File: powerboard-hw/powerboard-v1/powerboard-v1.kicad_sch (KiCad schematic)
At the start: 25 parts, among them J1 Conn_01x02, J2 PWR, J3 SIG, Q1 AO3401A, Q2 AO3400A, SW1 OS102011MA1Q, U1 TPS62842DGRR

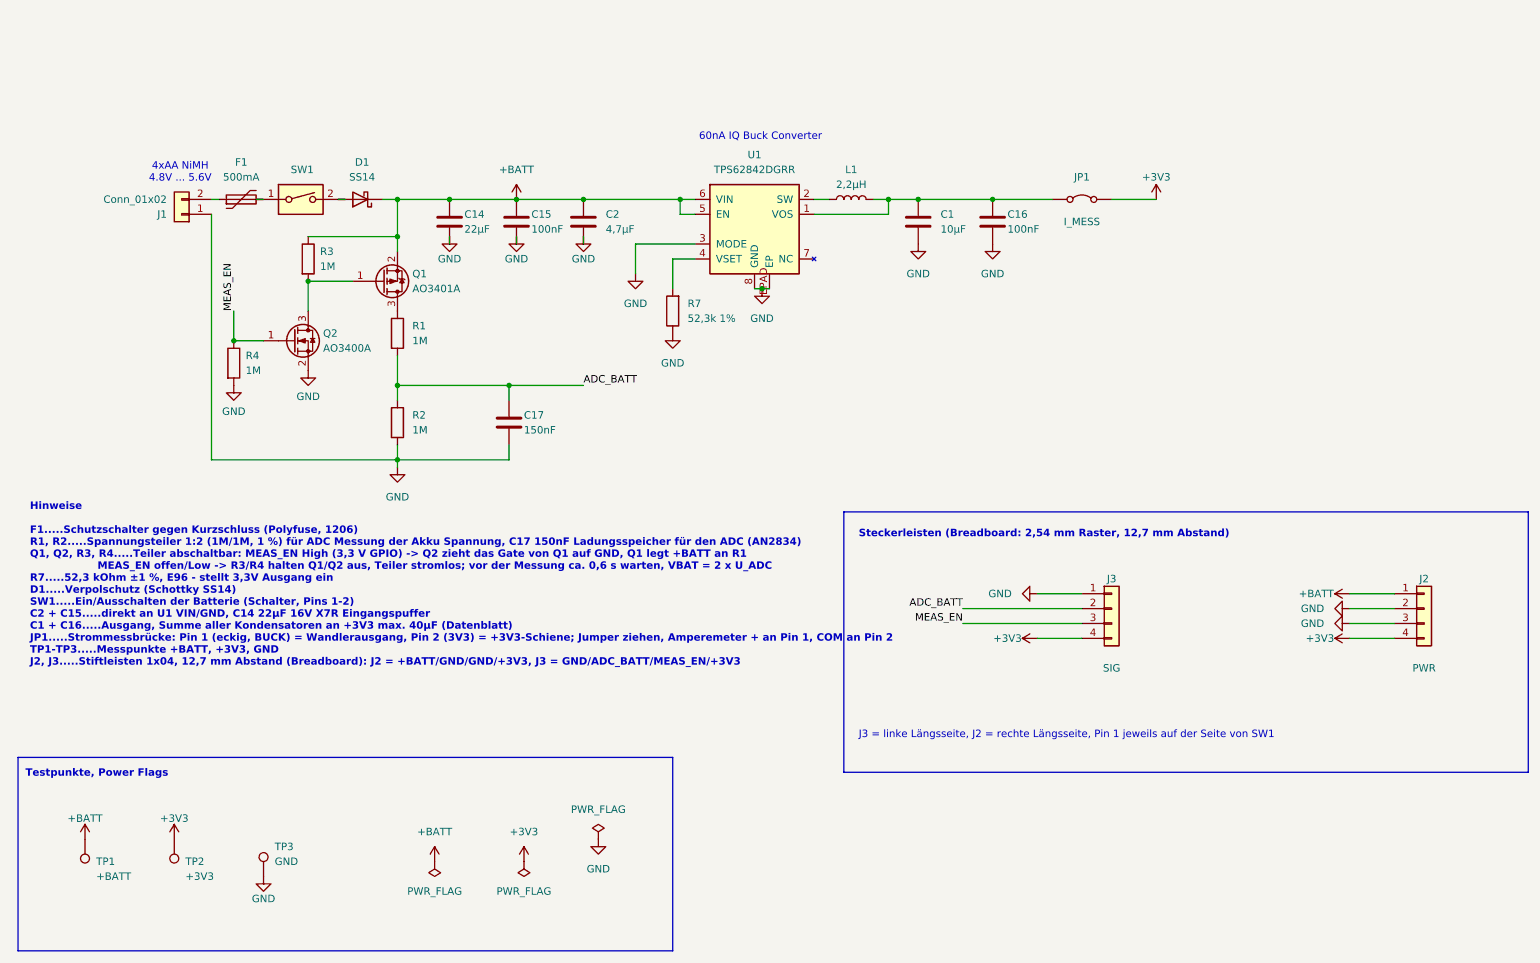
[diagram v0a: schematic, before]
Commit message: fix: SW1 switches the converter enable instead of the battery line
SW1 (C&K OS102011MA1Q) is rated 100 mA and sat in series with the
battery, which limited the module to about 120 mA. It now drives the
TPS62842 EN pin (net BUCK_EN): middle pin to EN, left pin to +BATT,
right pin to GND. Only the EN input current flows through it; the load
current goes J1 -> F1 -> D1 -> converter. F1 (500 mA hold) is now the
lowest limit, about 600 mA at 3.3 V.

ON/OFF direction from the C&K OS series datasheet (position 1 = 1-2,
position 2 = 2-3: the slider connects the middle pin to the outer pin
on its side): slider left = 2-3 = ON, slider right = 1-2 = OFF, printed
as ON / OFF at the two ends of the switch. OFF shuts the converter down
(25 nA typ.) and discharges +3V3; +BATT stays connected.

PCB: F1 connects straight to D1; BUCK_EN runs along the right edge with
one short B.Cu hop under the +BATT feed to J2. Schematic notes and
README (switch table, current limits, power-up steps) updated.

ERC: 0. DRC: 0 violations, 0 unconnected, schematic parity OK.

Co-Authored-By: Claude Opus 5.5 <noreply@anthropic.com>
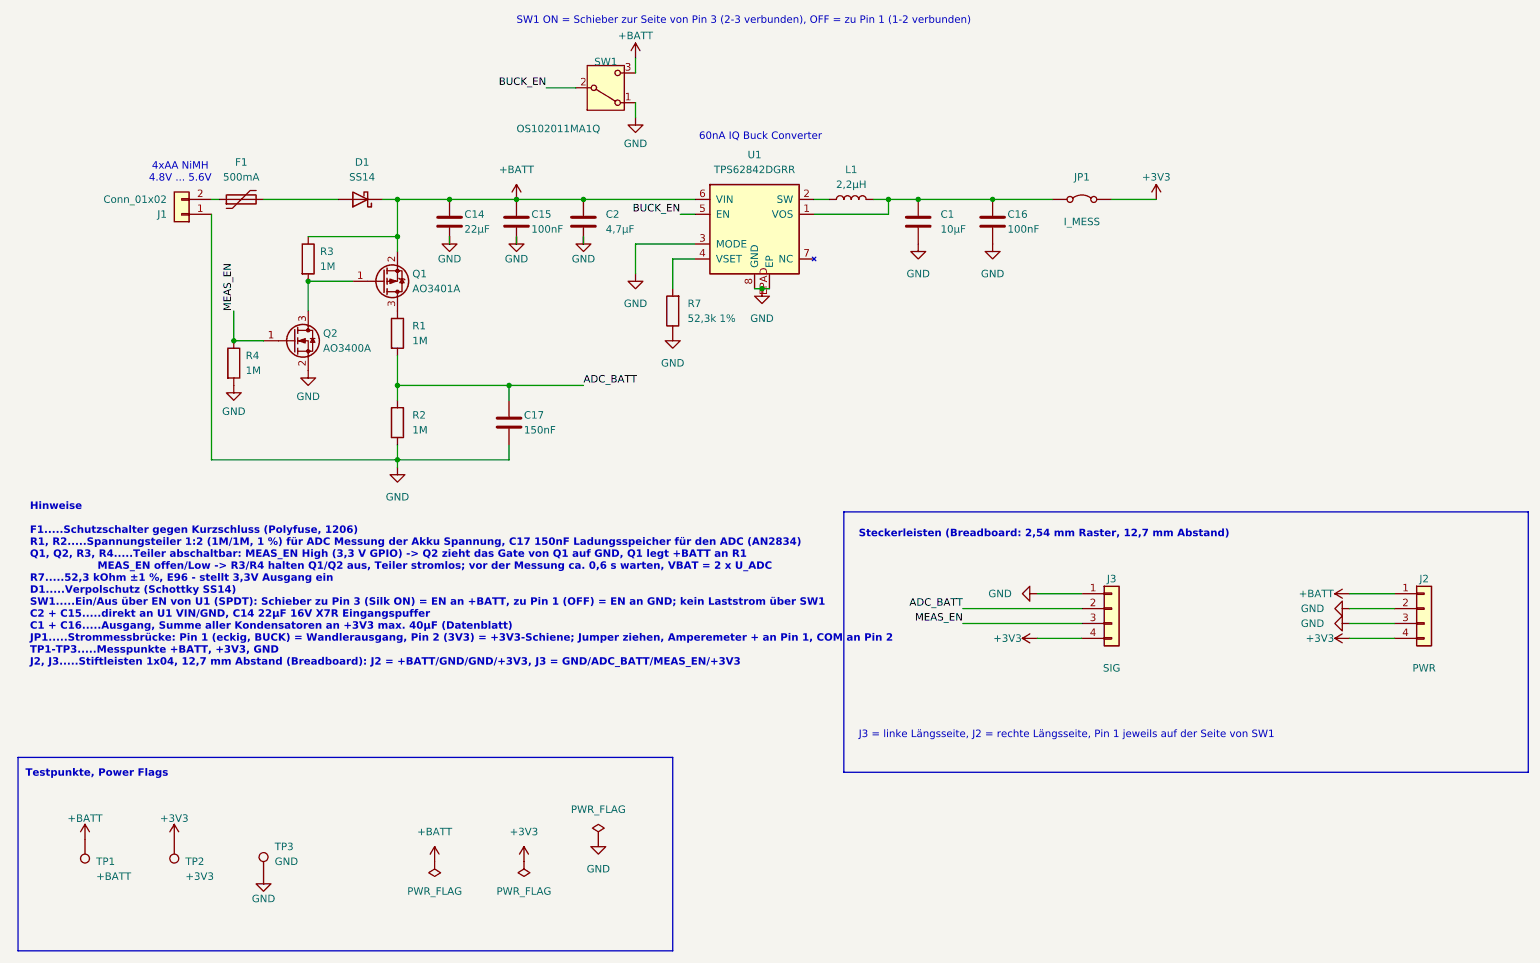
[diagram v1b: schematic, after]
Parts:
- removed J3: SIG, Connector_PinHeader_2.54mm:PinHeader_1x04_P2.54mm_Vertical, symbol Connector_Generic:Conn_01x04
- removed SW1: OS102011MA1Q, Button_Switch_THT:SW_Slide_SPDT_Angled_CK_OS102011MA1Q, symbol Switch:SW_DIP_x01
- added J2: PWR, Connector_PinHeader_2.54mm:PinHeader_1x04_P2.54mm_Vertical, symbol Connector_Generic:Conn_01x04
- added SW1: OS102011MA1Q, Button_Switch_THT:SW_Slide_SPDT_Angled_CK_OS102011MA1Q, symbol Switch:SW_SPDT
- J3: renamed from J2; value PWR -> SIG
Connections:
- net +3V3: now also J2.4 (Pin_4)
- net +BATT: now also J2.1 (Pin_1), SW1.3 (C); no longer J3.1 (Pin_1), U1.5 (EN)
- net ADC_BATT: now also J3.2 (Pin_2)
- net GND: now also J3.1 (Pin_1), J2.2 (Pin_2), J2.3 (Pin_3), SW1.1 (A); no longer J3.2 (Pin_2), J3.3 (Pin_3)
- net MEAS_EN: now also J3.3 (Pin_3)
- net at F1.2: now also D1.2 (A)
- new net BUCK_EN: SW1.2 (B), U1.5 (EN)
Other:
- note added: "SW1 ON = Schieber zur Seite von Pin 3 (2-3 verbunden), OFF = zu Pin 1 (1-2 verbunden)"
- moved on the sheet: J3

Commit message: fix: battery divider R1/R2 100k instead of 1M
The divider is switched off by Q1 between measurements, so it no longer
needs megaohm values. With 100k/100k the settling of C17 (150 nF)
drops from tau = 75 ms to 7.5 ms: about 65 ms before the ADC reading
instead of 0.6 s. Current while measuring is about 37 uA, the charge
per measurement is lower than before (about 4 uC vs 7 uC).

R3/R4 stay 1M. Board geometry unchanged (tracks, vias, pads, silk,
fills identical); only the values in schematic, BOM, position file and
Gerber attributes change. Schematic notes and README timing updated.

ERC: 0. DRC: 0 violations, 0 unconnected, schematic parity OK.

Co-Authored-By: Claude Opus 5.5 <noreply@anthropic.com>
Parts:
- R1, R2: value 1M -> 100k
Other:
- note added: "Hinweise F1.....Schutzschalter gegen Kurzschluss (Polyfuse, 1206) R1, R2.....Spannungsteiler 1:2 (100k/100k, 1 %) für ADC Messung der Akku Spannung, C17 150nF Ladungsspeicher für den ADC (AN2834) Q1, Q2, R3, R4.....Teiler abschaltbar: MEAS_EN High (3,3 V GPIO) -> Q2 zieht das Gate von Q1 auf GND, Q1 legt +BATT an R1 MEAS_EN offen/Low -> R3/R4 halten Q1/Q2 aus, Teiler stromlos; vor der Messung ca.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"
- note removed: "Hinweise F1.....Schutzschalter gegen Kurzschluss (Polyfuse, 1206) R1, R2.....Spannungsteiler 1:2 (1M/1M, 1 %) für ADC Messung der Akku Spannung, C17 150nF Ladungsspeicher für den ADC (AN2834) Q1, Q2, R3, R4.....Teiler abschaltbar: MEAS_EN High (3,3 V GPIO) -> Q2 zieht das Gate von Q1 auf GND, Q1 legt +BATT an R1 MEAS_EN offen/Low -> R3/R4 halten Q1/Q2 aus, Teiler stromlos; vor der Messung ca. 0,6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"
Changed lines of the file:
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@@
 		)
 	)
-	(text "Hinweise\n\nF1.....Schutzschalter gegen Kurzschluss (Polyfuse, 1206)\nR1, R2.....Spannungsteiler 1:2 (1M/1M, 1 %) für ADC Messung der Akku Spannung, C17 150nF Ladungsspeicher für den ADC (AN2834)\nQ1, Q2, R3, R4.....Teiler abschaltbar: MEAS_EN High (3,3 V GPIO) -> Q2 zieht das Gate von Q1 auf GND, Q1 legt +BATT an R1\n                   MEAS_EN offen/Low -> R3/R4 halten Q1/Q2 aus, Teiler stromlos; vor der Messung ca. 0,6 s warten, VBAT = 2 x U_ADC\nR7.....52,3 kOhm ±1 %, E96 - stellt 3,3V Ausgang ein\nD1.....Verpolschutz (Schottky SS14)\nSW1.....Ein/Aus über EN von U1 (SPDT): Schieber zu Pin 3 (Silk ON) = EN an +BATT, zu Pin 1 (OFF) = EN an GND; kein Laststrom über SW1\nC2 + C15.....direkt an U1 VIN/GND, C14 22µF 16V X7R Eingangspuffer\nC1 + C16.....Ausgang, Summe aller Kondensatoren an +3V3 max. 40µF (Datenblatt)\nJP1.....Strommessbrücke: Pin 1 (eckig, BUCK) = Wandlerausgang, Pin 2 (3V3) = +3V3-Schiene; Jumper ziehen, Amperemeter + an Pin 1, COM an Pin 2\nTP1-TP3.....Messpunkte +BATT, +3V3, GND\nJ2, J3.....Stiftleisten 1x04, 12,7 mm Abstand (Breadboard): J2 = +BATT/GND/GND/+3V3, J3 = GND/ADC_BATT/MEAS_EN/+3V3\n"
+	(text "Hinweise\n\nF1.....Schutzschalter gegen Kurzschluss (Polyfuse, 1206)\nR1, R2.....Spannungsteiler 1:2 (100k/100k, 1 %) für ADC Messung der Akku Spannung, C17 150nF Ladungsspeicher für den ADC (AN2834)\nQ1, Q2, R3, R4.....Teiler abschaltbar: MEAS_EN High (3,3 V GPIO) -> Q2 zieht das Gate von Q1 auf GND, Q1 legt +BATT an R1\n                   MEAS_EN offen/Low -> R3/R4 halten Q1/Q2 aus, Teiler stromlos; vor der Messung ca. 60 ms warten, VBAT = 2 x U_ADC\nR7.....52,3 kOhm ±1 %, E96 - stellt 3,3V Ausgang ein\nD1.....Verpolschutz (Schottky SS14)\nSW1.....Ein/Aus über EN von U1 (SPDT): Schieber zu Pin 3 (Silk ON) = EN an +BATT, zu Pin 1 (OFF) = EN an GND; kein Laststrom über SW1\nC2 + C15.....direkt an U1 VIN/GND, C14 22µF 16V X7R Eingangspuffer\nC1 + C16.....Ausgang, Summe aller Kondensatoren an +3V3 max. 40µF (Datenblatt)\nJP1.....Strommessbrücke: Pin 1 (eckig, BUCK) = Wandlerausgang, Pin 2 (3V3) = +3V3-Schiene; Jumper ziehen, Amperemeter + an Pin 1, COM an Pin 2\nTP1-TP3.....Messpunkte +BATT, +3V3, GND\nJ2, J3.....Stiftleisten 1x04, 12,7 mm Abstand (Breadboard): J2 = +BATT/GND/GND/+3V3, J3 = GND/ADC_BATT/MEAS_EN/+3V3\n"
 		(exclude_from_sim no)
 		(at 21.082 128.016 0)
@@
 			)
 		)
-		(property "Value" "1M"
+		(property "Value" "100k"
 			(at 86.36 101.5999 0)
 			(show_name no)
@@
 			)
 		)
-		(property "Value" "1M"
+		(property "Value" "100k"
 			(at 86.36 86.3599 0)
 			(show_name no)
